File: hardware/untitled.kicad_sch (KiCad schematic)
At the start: 29 parts, among them U3 MC7812BDTRKG, U4 AZ1117CD-3.3TRG1, U5 AZ1117CD-3.3TRG1

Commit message: minor hardware refactoring
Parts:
- added R26, R28: 2K2, Resistor_SMD:R_0603_1608Metric, symbol Device:R
- added R27, R29: 660R, Resistor_SMD:R_0603_1608Metric, symbol Device:R
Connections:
- net 10.94VDC: now also R28.1
- net 16.33VDC: now also R26.1
- net GND: now also R27.2, R29.2
- new net: R28.2, R29.1
- new net: R26.2, R27.1
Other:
- moved on the sheet: C10, C11, C12, C13, C8, C9, D11, D12, D13, R13, R14, R15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

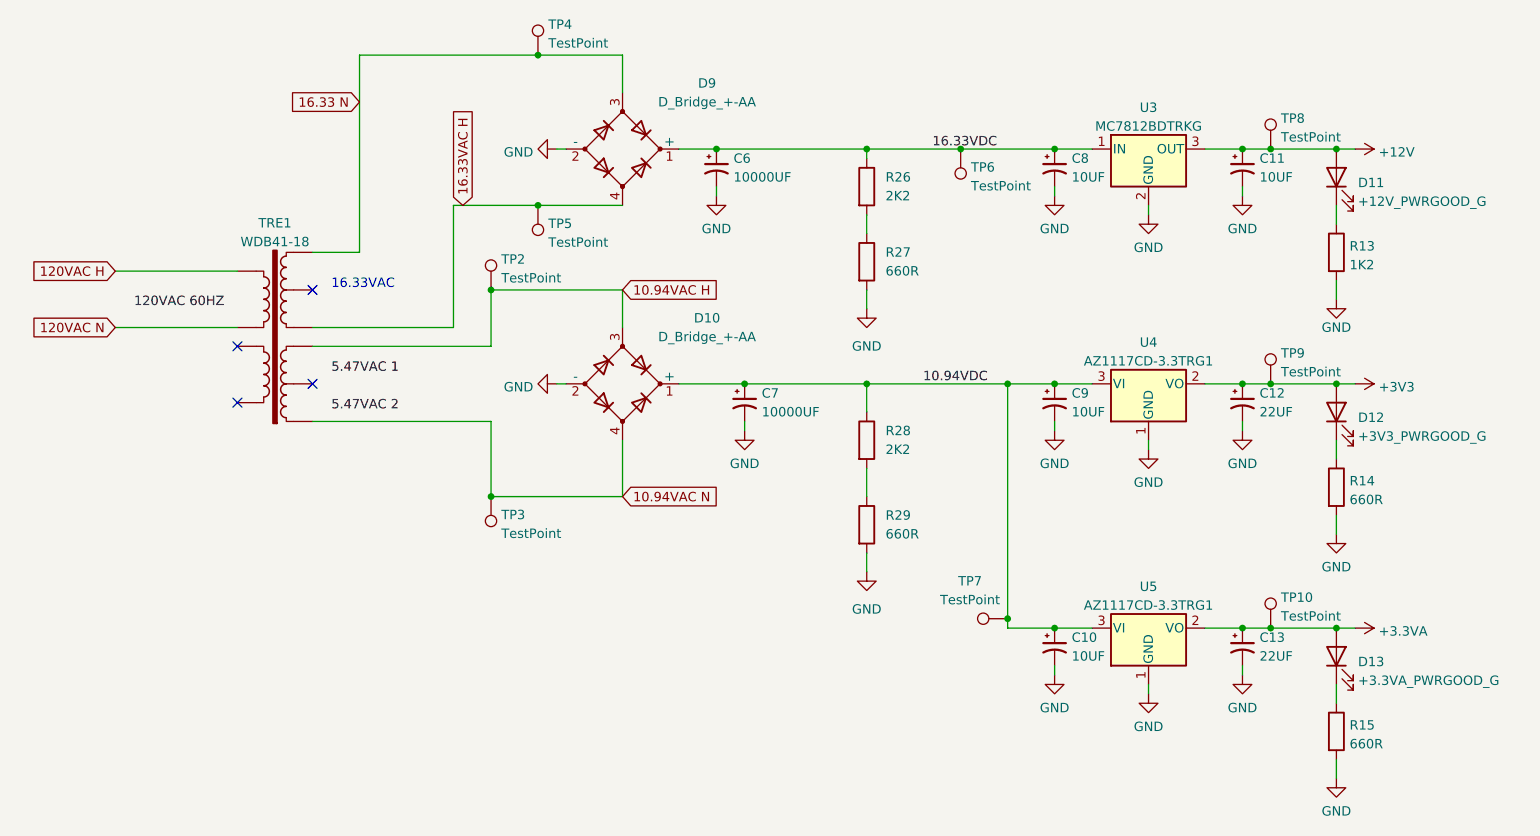
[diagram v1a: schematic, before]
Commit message: major hardware refctoring to use modern parts that are still being made
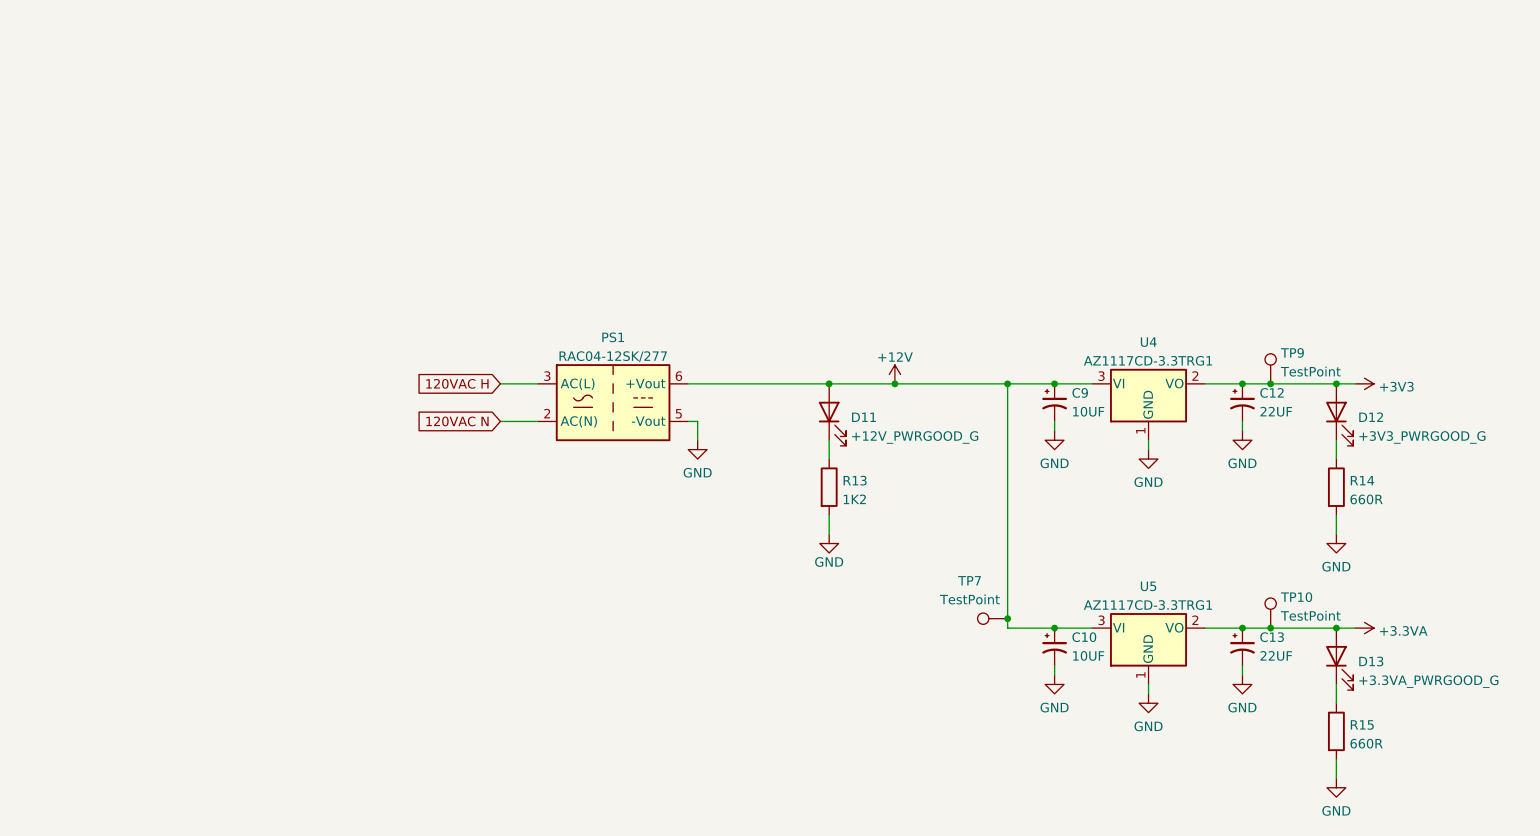
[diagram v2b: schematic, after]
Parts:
- removed C11, C8: 10UF, Capacitor_SMD:C_0603_1608Metric, symbol Device:C_Polarized_Small_US
- removed C6, C7: 10000UF, Capacitor_THT:CP_Radial_D35.0mm_P10.00mm_SnapIn, symbol Device:C_Polarized_Small_US
- removed D10, D9: D_Bridge_+-AA, EXTRA:DF01S-TDICT-ND, symbol Device:D_Bridge_+-AA
- removed R26, R28: 2K2, Resistor_SMD:R_0603_1608Metric, symbol Device:R
- removed R27, R29: 660R, Resistor_SMD:R_0603_1608Metric, symbol Device:R
- removed TP2, TP3, TP4, TP5, TP6, TP8: TestPoint, TestPoint:TestPoint_Pad_D2.0mm, symbol Connector:TestPoint
- removed TRE1: WDB41-18, EXTRA:WDB41-18, symbol Transformer:TRANSF7
- removed U3: MC7812BDTRKG, Package_TO_SOT_SMD:TO-252-3_TabPin2, symbol Regulator_Linear:L7812
- added PS1: RAC04-12SK/277, EXTRA:CONV_RAC04-12SK_277, symbol Converter_ACDC:RAC04-12SGA
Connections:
- net 10.94VDC is gone; now on net +12V: C10.1, C9.1, TP7.1, U4.3 (VI), U5.3 (VI)
- net +12V: now also PS1.6 (+Vout)
- net 120VAC H: now also PS1.3 (AC(L))
- net 120VAC N: now also PS1.2 (AC(N))
- net GND: now also PS1.5 (-Vout)
- no-connect marks 4 -> 0
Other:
- note removed: "16.33VAC"
- moved on the sheet: D11, R13
